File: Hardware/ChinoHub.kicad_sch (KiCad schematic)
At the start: 0 parts

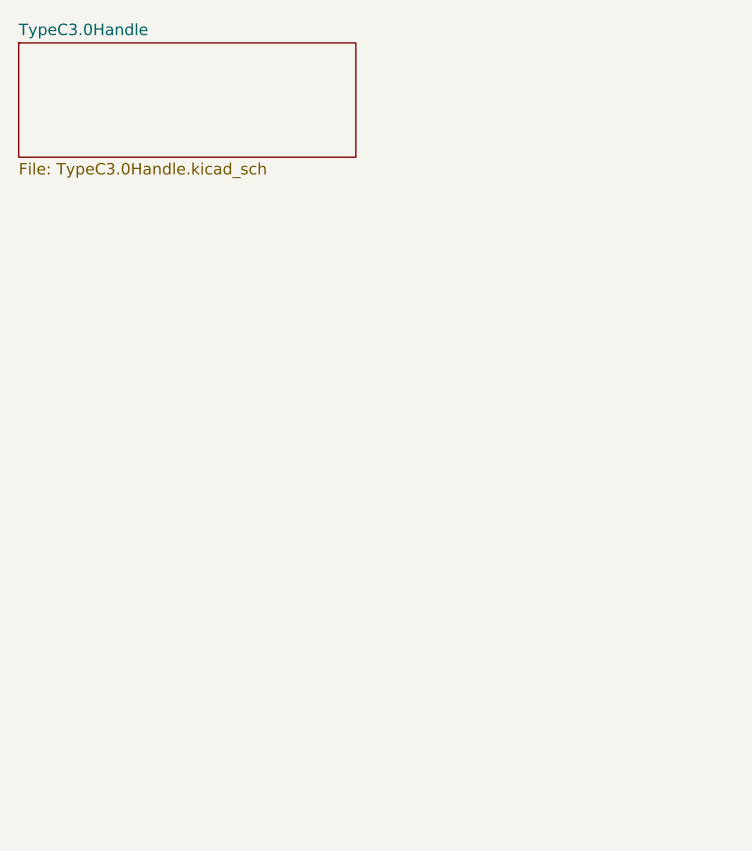
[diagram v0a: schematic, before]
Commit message: 完成TypeC转HDMI部分
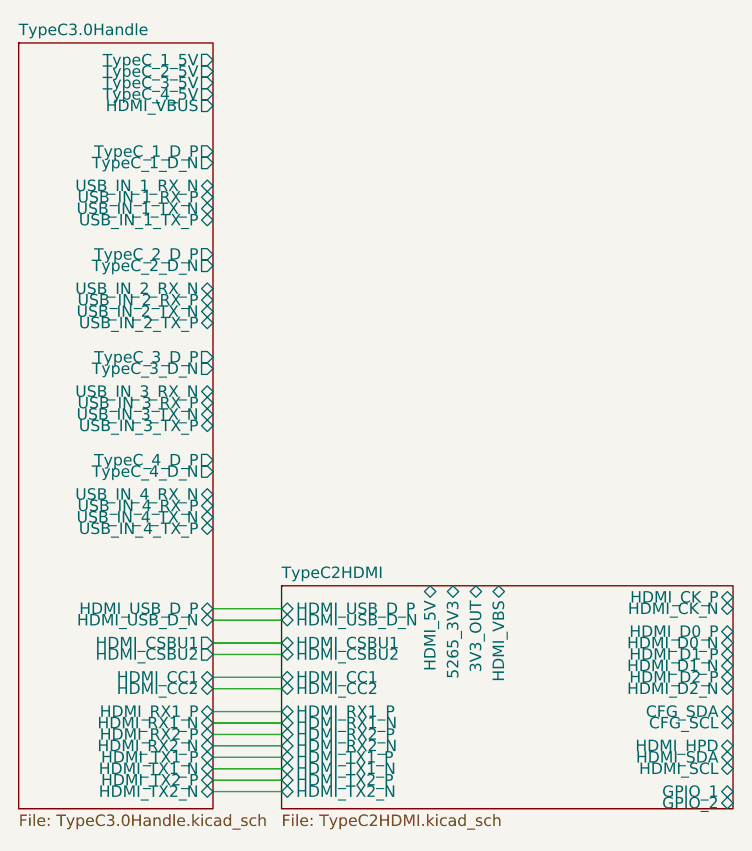
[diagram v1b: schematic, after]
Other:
- added sheet TypeC2HDMI (TypeC2HDMI.kicad_sch)
- sheet TypeC3.0Handle ports: added HDMI_CC1, HDMI_CC2, HDMI_CSBU1, HDMI_CSBU2, HDMI_RX1_N, HDMI_RX1_P, HDMI_RX2_N, HDMI_RX2_P, HDMI_TX1_N, HDMI_TX1_P, HDMI_TX2_N, HDMI_TX2_P, HDMI_USB_D_N, HDMI_USB_D_P, HDMI_VBUS, TypeC_1_5V, TypeC_1_D_N, TypeC_1_D_P, TypeC_2_5V, TypeC_2_D_N, TypeC_2_D_P, TypeC_3_5V, TypeC_3_D_N, TypeC_3_D_P, TypeC_4_5V, TypeC_4_D_N, TypeC_4_D_P, USB_IN_1_RX_N, USB_IN_1_RX_P, USB_IN_1_TX_N, USB_IN_1_TX_P, USB_IN_2_RX_N, USB_IN_2_RX_P, USB_IN_2_TX_N, USB_IN_2_TX_P, USB_IN_3_RX_N, USB_IN_3_RX_P, USB_IN_3_TX_N, USB_IN_3_TX_P, USB_IN_4_RX_N, USB_IN_4_RX_P, USB_IN_4_TX_N, USB_IN_4_TX_P; removed none

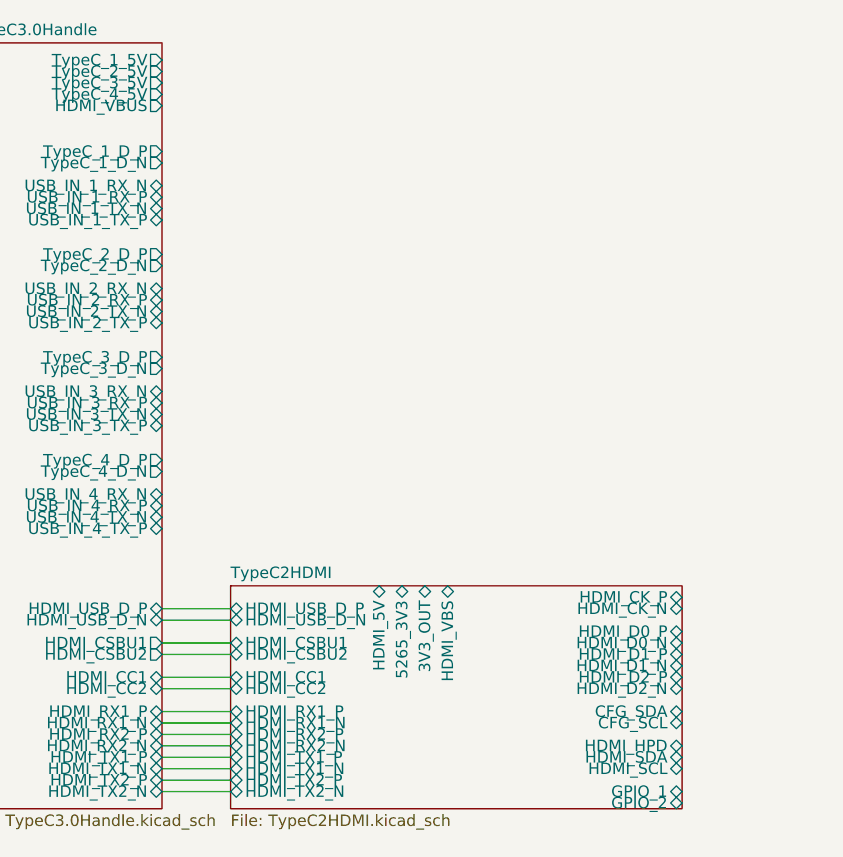
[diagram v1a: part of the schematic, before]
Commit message: 完成HUB部分原理图绘制
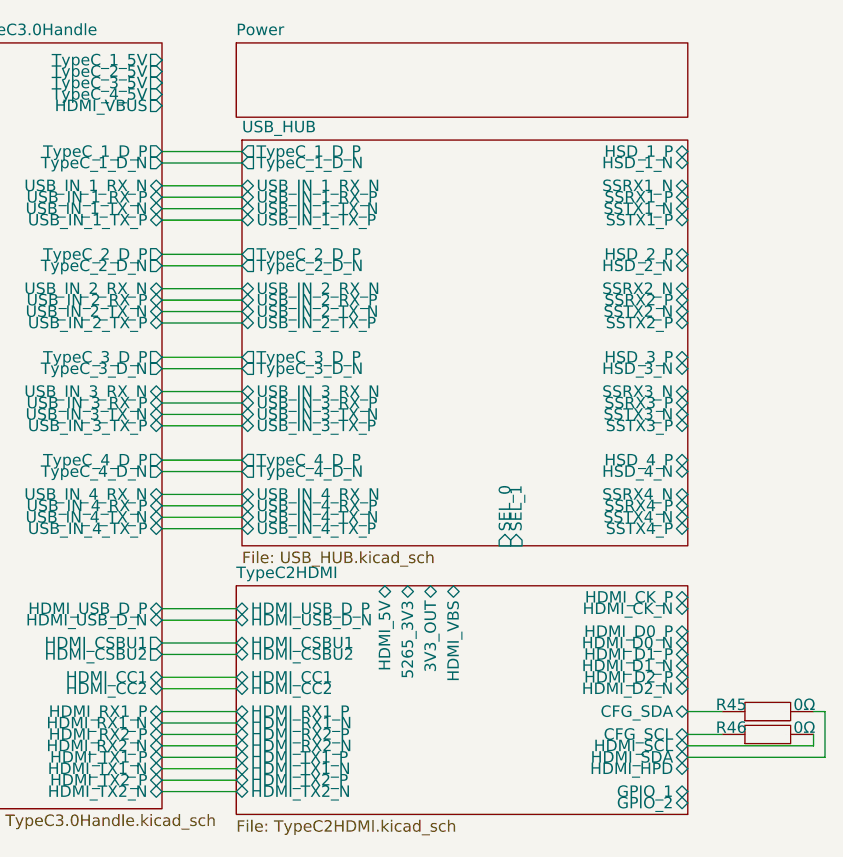
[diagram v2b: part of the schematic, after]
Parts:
- added R45, R46: 0Ω, persional_library:R0603, symbol persional_library:R0603
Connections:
- net TypeC2HDMI/CFG_SCL: now also R46.1
- net TypeC2HDMI/CFG_SDA: now also R45.1
- net TypeC2HDMI/HDMI_SCL: now also R46.2
- net TypeC2HDMI/HDMI_SDA: now also R45.2
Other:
- added sheet Power (Power.kicad_sch)
- added sheet USB_HUB (USB_HUB.kicad_sch)

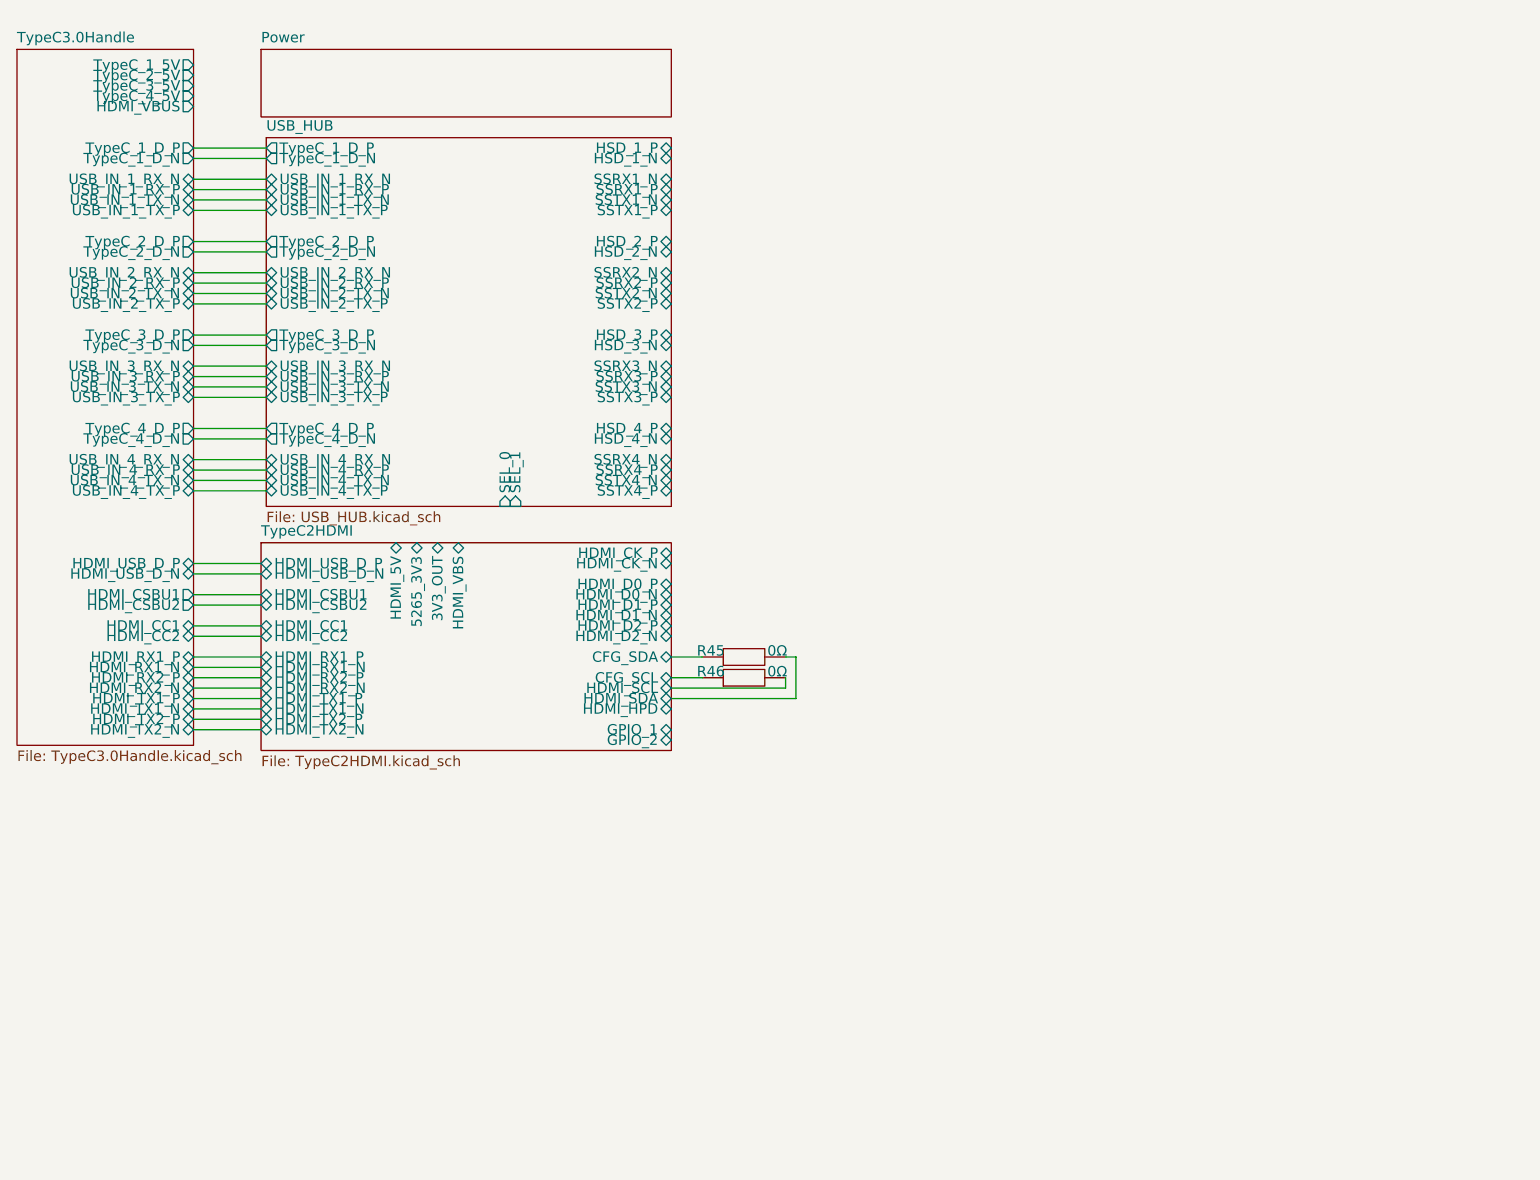
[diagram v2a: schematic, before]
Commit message: 完成HUB部分基础内容
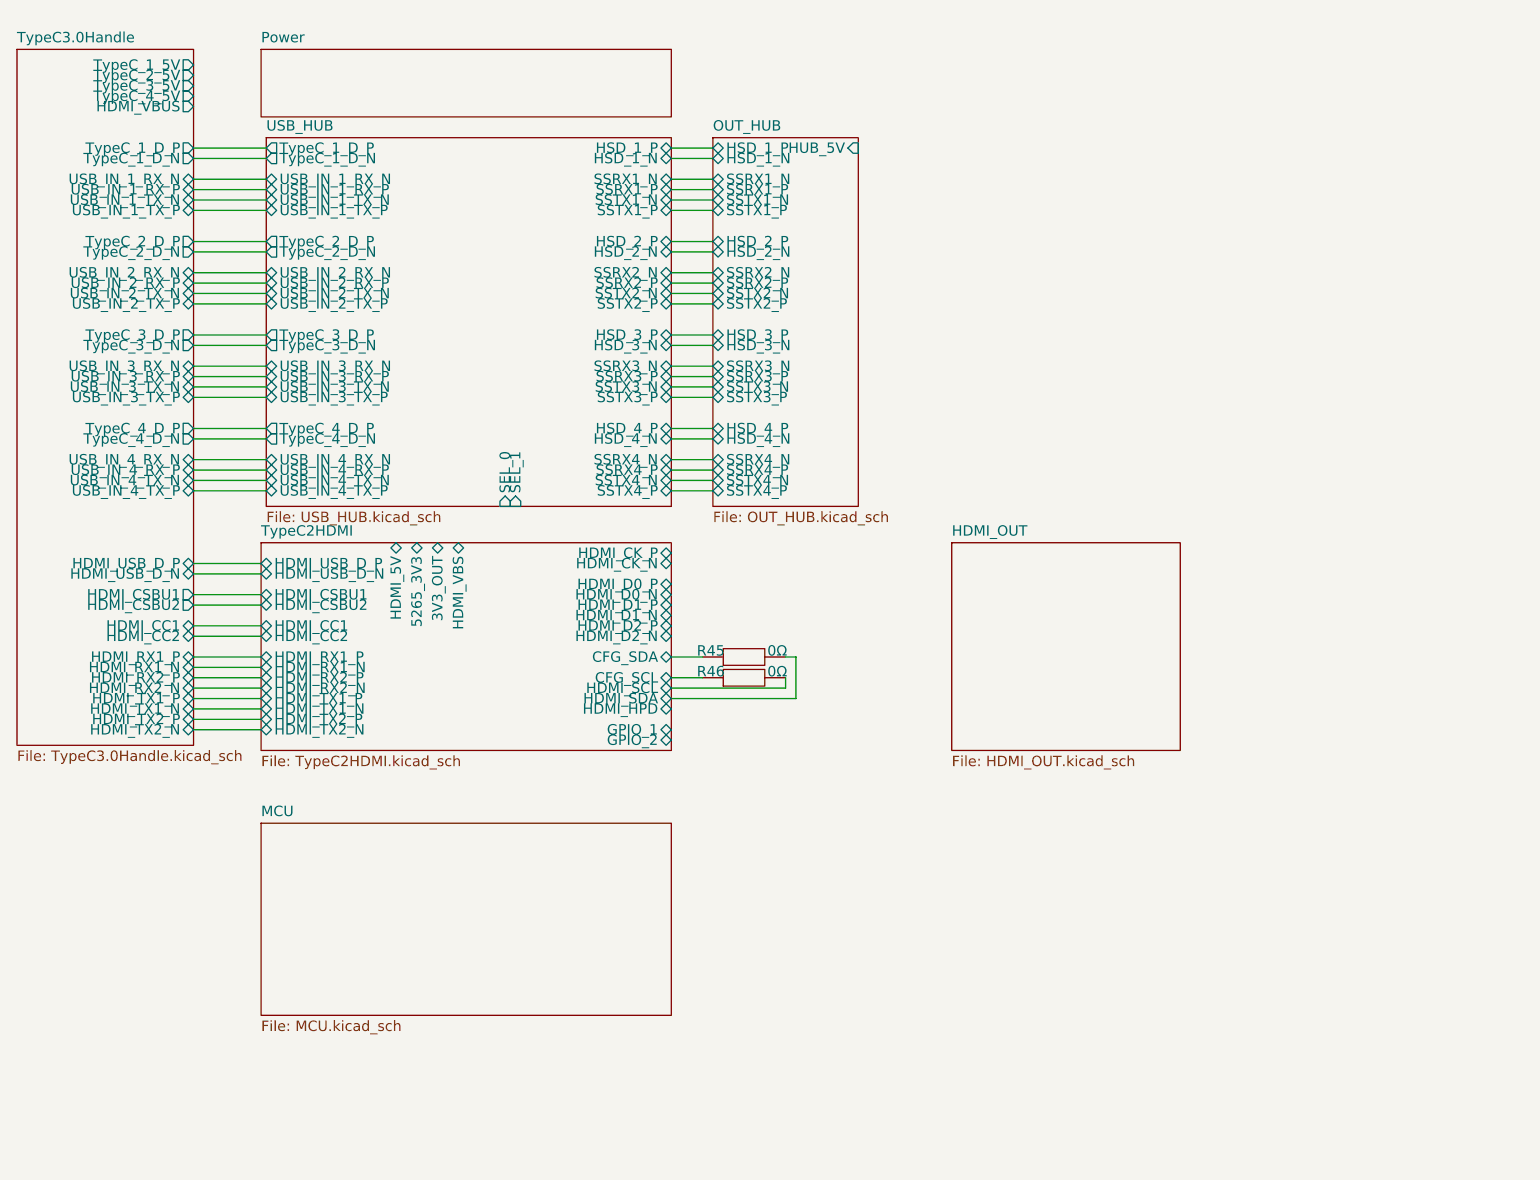
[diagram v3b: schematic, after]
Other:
- added sheet HDMI_OUT (HDMI_OUT.kicad_sch)
- added sheet MCU (MCU.kicad_sch)
- added sheet OUT_HUB (OUT_HUB.kicad_sch)

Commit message: 完成除MCU外的设计
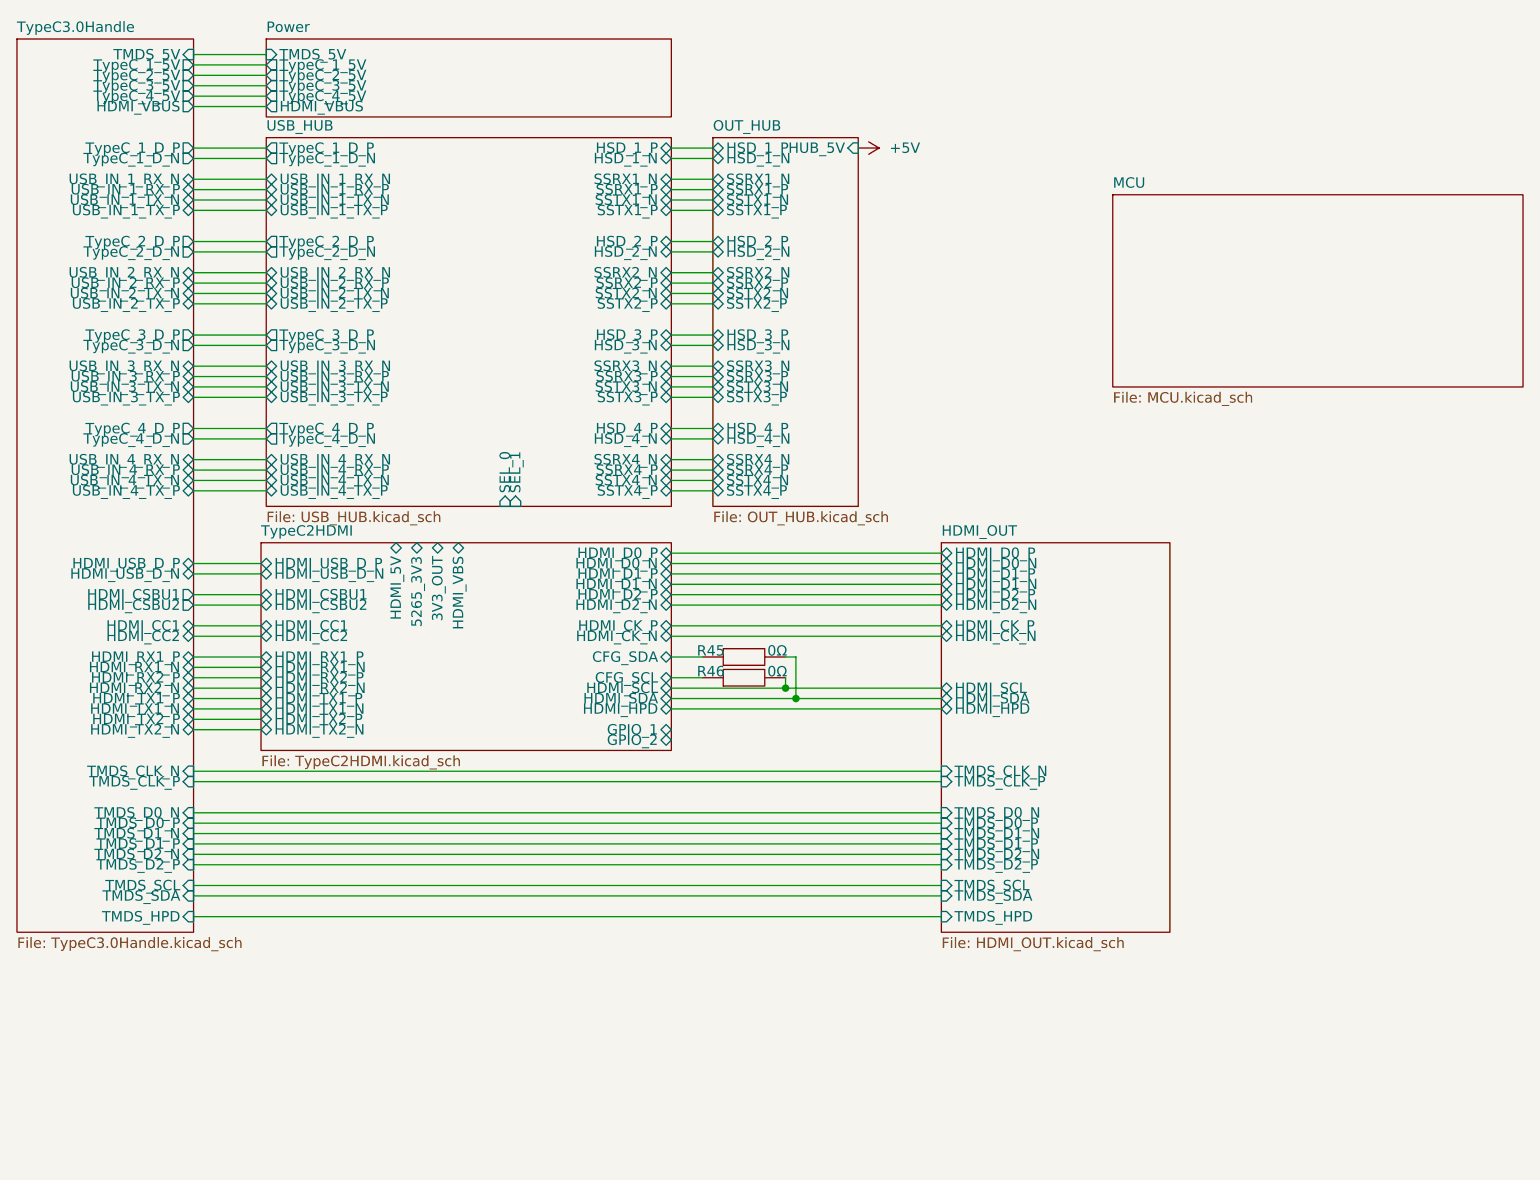
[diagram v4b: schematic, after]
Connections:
- net TypeC2HDMI/HDMI_SCL renamed HDMI_OUT/HDMI_SCL
- net TypeC2HDMI/HDMI_SDA renamed HDMI_OUT/HDMI_SDA
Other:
- sheet HDMI_OUT ports: added HDMI_CK_N, HDMI_CK_P, HDMI_D0_N, HDMI_D0_P, HDMI_D1_N, HDMI_D1_P, HDMI_D2_N, HDMI_D2_P, HDMI_HPD, HDMI_SCL, HDMI_SDA, TMDS_CLK_N, TMDS_CLK_P, TMDS_D0_N, TMDS_D0_P, TMDS_D1_N, TMDS_D1_P, TMDS_D2_N, TMDS_D2_P, TMDS_HPD, TMDS_SCL, TMDS_SDA; removed none
- sheet Power ports: added HDMI_VBUS, TMDS_5V, TypeC_1_5V, TypeC_2_5V, TypeC_3_5V, TypeC_4_5V; removed none
- sheet TypeC3.0Handle ports: added TMDS_5V, TMDS_CLK_N, TMDS_CLK_P, TMDS_D0_N, TMDS_D0_P, TMDS_D1_N, TMDS_D1_P, TMDS_D2_N, TMDS_D2_P, TMDS_HPD, TMDS_SCL, TMDS_SDA; removed none

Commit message: complete sch
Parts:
- added D7, D9: ~, persional_library:SOD-323F_L1.7-W1.3-LS2.5-R-RD, symbol persional_library:Diode_1N4148WSL
- added R81, R84, R87, R88: 2.2kΩ, persional_library:R0603, symbol persional_library:R0603
- added R90, R91: 10kΩ, persional_library:R0603, symbol persional_library:R0603
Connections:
- net +5V: now also D7.2, D9.2
- net HDMI_OUT/HDMI_SCL: now also R84.2
- net HDMI_OUT/HDMI_SDA: now also R81.2
- net HDMI_OUT/TMDS_SCL: now also R87.2
- net HDMI_OUT/TMDS_SDA: now also R88.2
- new net: D7.1, R81.1, R84.1
- new net: D9.1, R87.1, R88.1
- new net +3V3: R90.2, R91.2
- new net HDMI_OUT/HDMI_SEL1: R90.1
- new net HDMI_OUT/HDMI_SEL2: R91.1
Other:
- sheet HDMI_OUT ports: added HDMI_EN, HDMI_SEL1, HDMI_SEL2; removed none
- sheet MCU ports: added GPIO_1, GPIO_2, HMDI_EN, HMDI_SEL1, HMDI_SEL2, HUB_SEL0, HUB_SEL1; removed none
- sheet TypeC2HDMI ports: added none; removed 3V3_OUT, 5265_3V3
